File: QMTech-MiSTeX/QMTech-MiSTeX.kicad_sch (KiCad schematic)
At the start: 20 parts, among them J1 RPi_GPIO, J2 MiSTer SDRAM Module, J3 Conn_02x32_Odd_Even, J4 Conn_02x32_Odd_Even, J5 Conn_01x06_Male, J7 Conn_01x05_Pin, J8 USB_C_Receptacle_USB2.0, U5 ZGY133/T10(PLT)

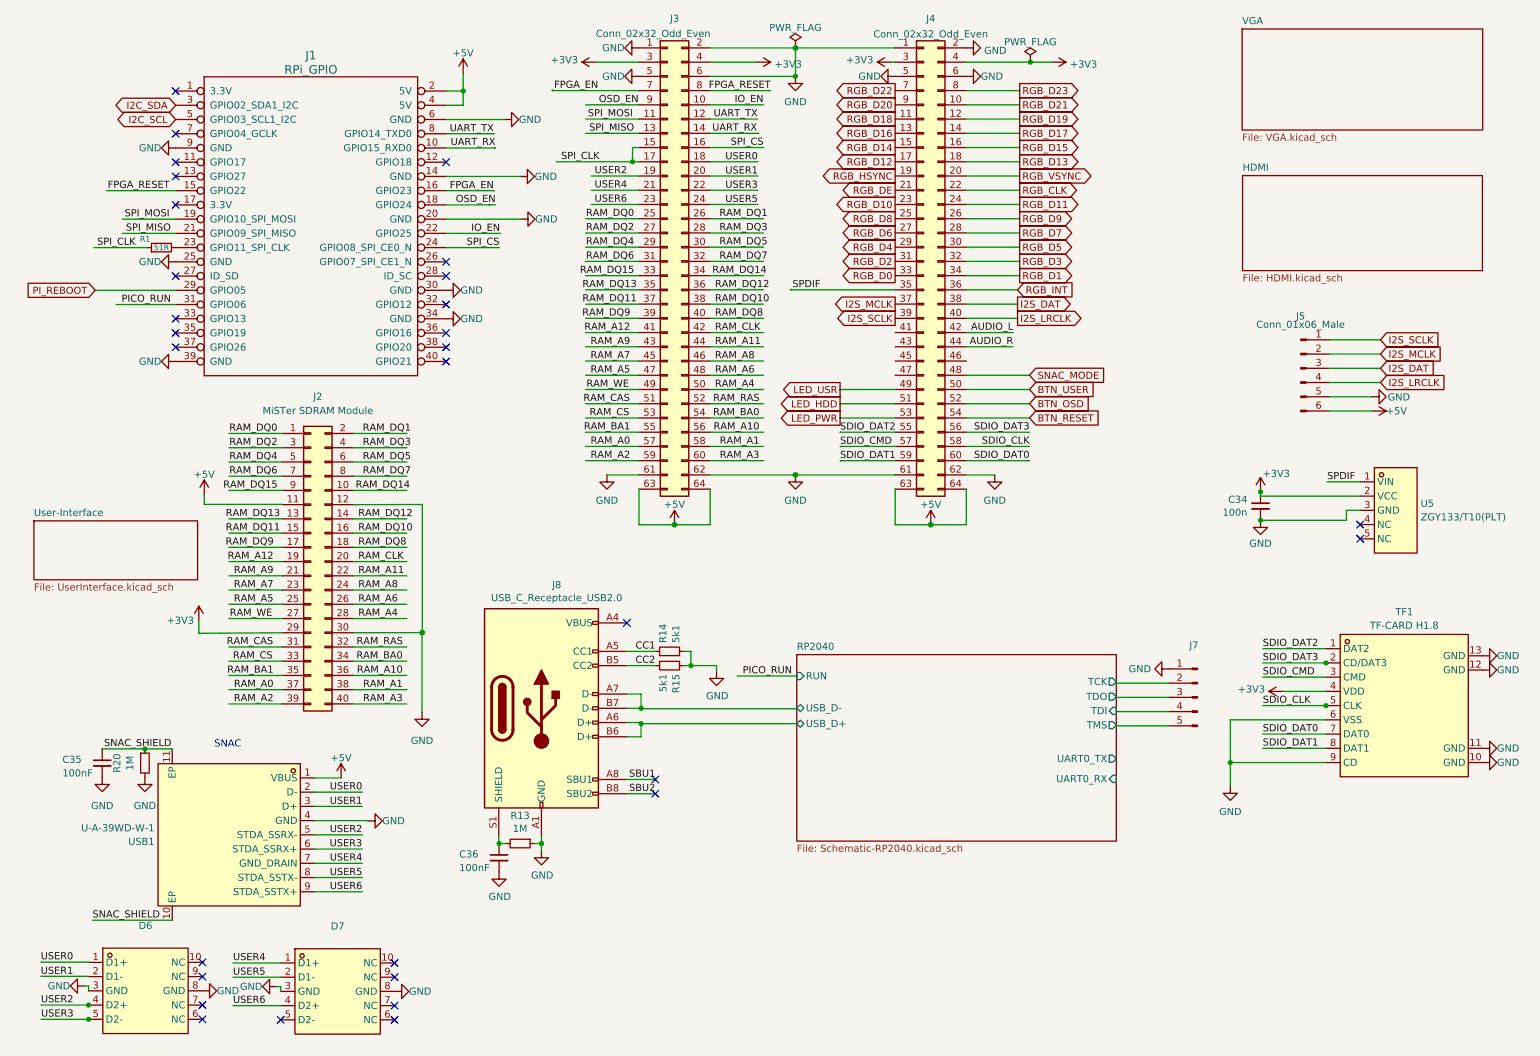
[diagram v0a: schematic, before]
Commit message: move SNAC into its own sheet
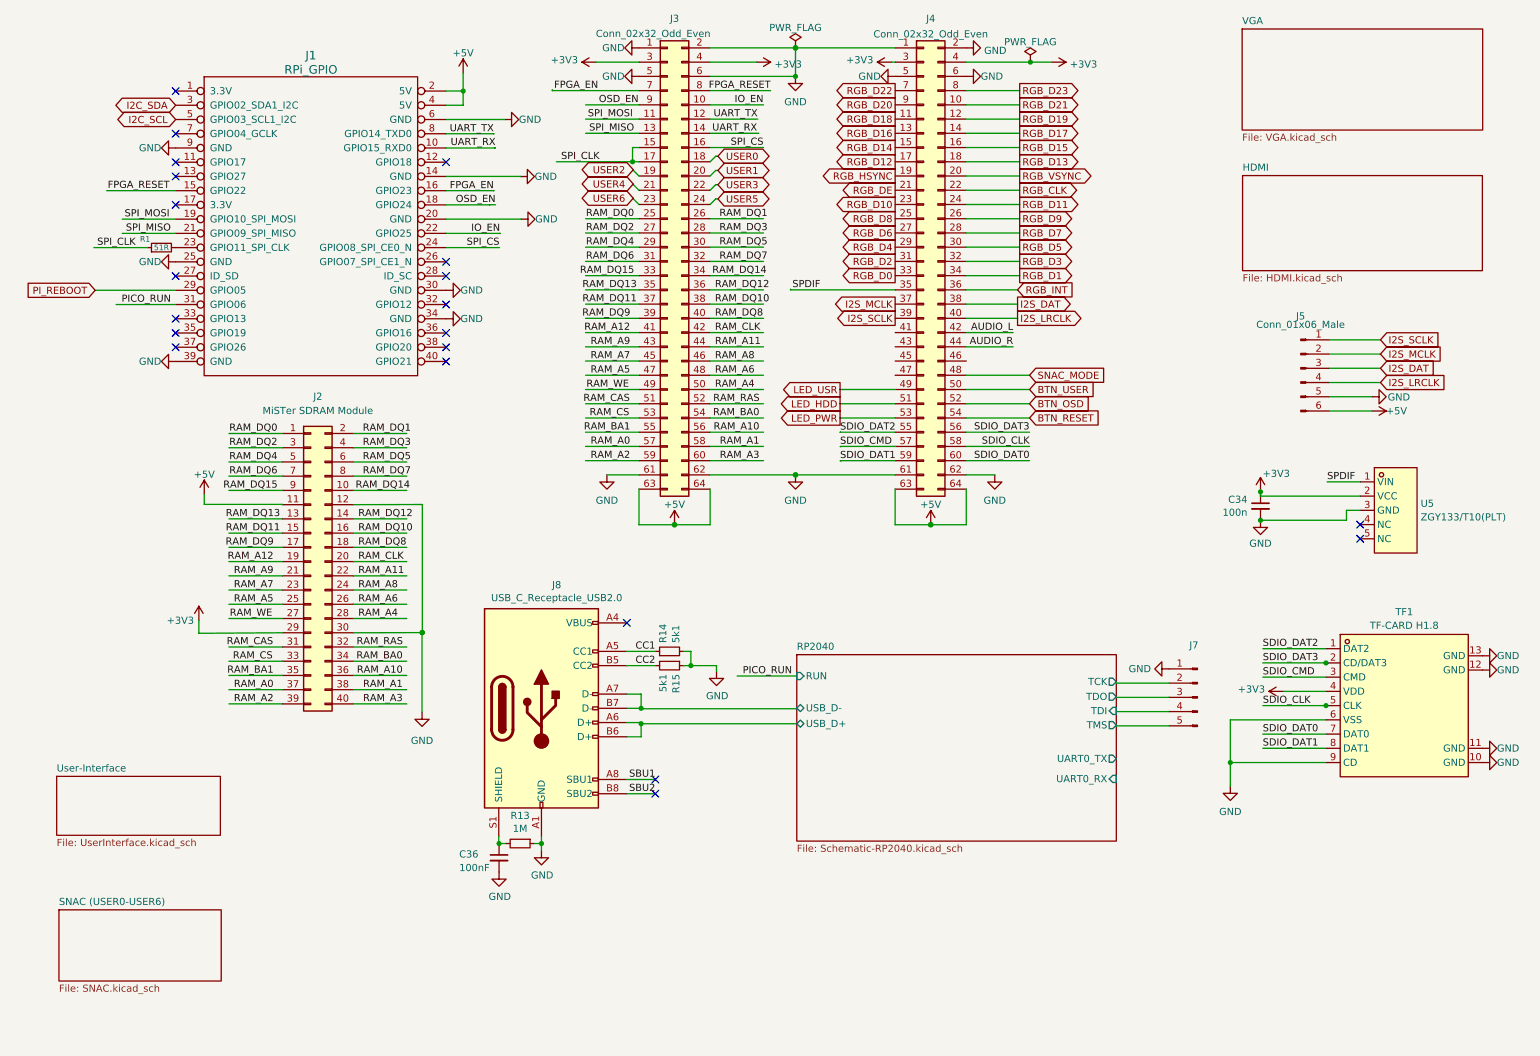
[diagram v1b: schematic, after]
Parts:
- removed C35: 100nF, C_0402_1005Metric, symbol jlcpcb-basic-mlcc-0402:100nF
- removed D6, D7: TPD4E05U06DQAR_C2972498, easyeda2kicad:DFN2510-10_L2.5-W1.0-P0.50-BL, symbol easyeda2kicad:TPD4E05U06DQAR_C2972498
- removed R20: 1M, Resistor_SMD:R_0603_1608Metric, symbol Device:R_Small
- removed USB1: U-A-39WD-W-1, easyeda2kicad:USB-A-SMD_U-A-39WD-W-1, symbol easyeda2kicad:U-A-39WD-W-1
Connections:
- net USER0: now also J3.18 (Pin_18)
- net USER1: now also J3.20 (Pin_20)
- net USER3: now also J3.22 (Pin_22)
- net USER5: now also J3.24 (Pin_24)
- no-connect marks 30 -> 21
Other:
- added sheet SNAC (USER0-USER6) (SNAC.kicad_sch)
- note removed: "SNAC"

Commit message: apply review notes from somhi, move audio into its own subsheet, add analog audio out
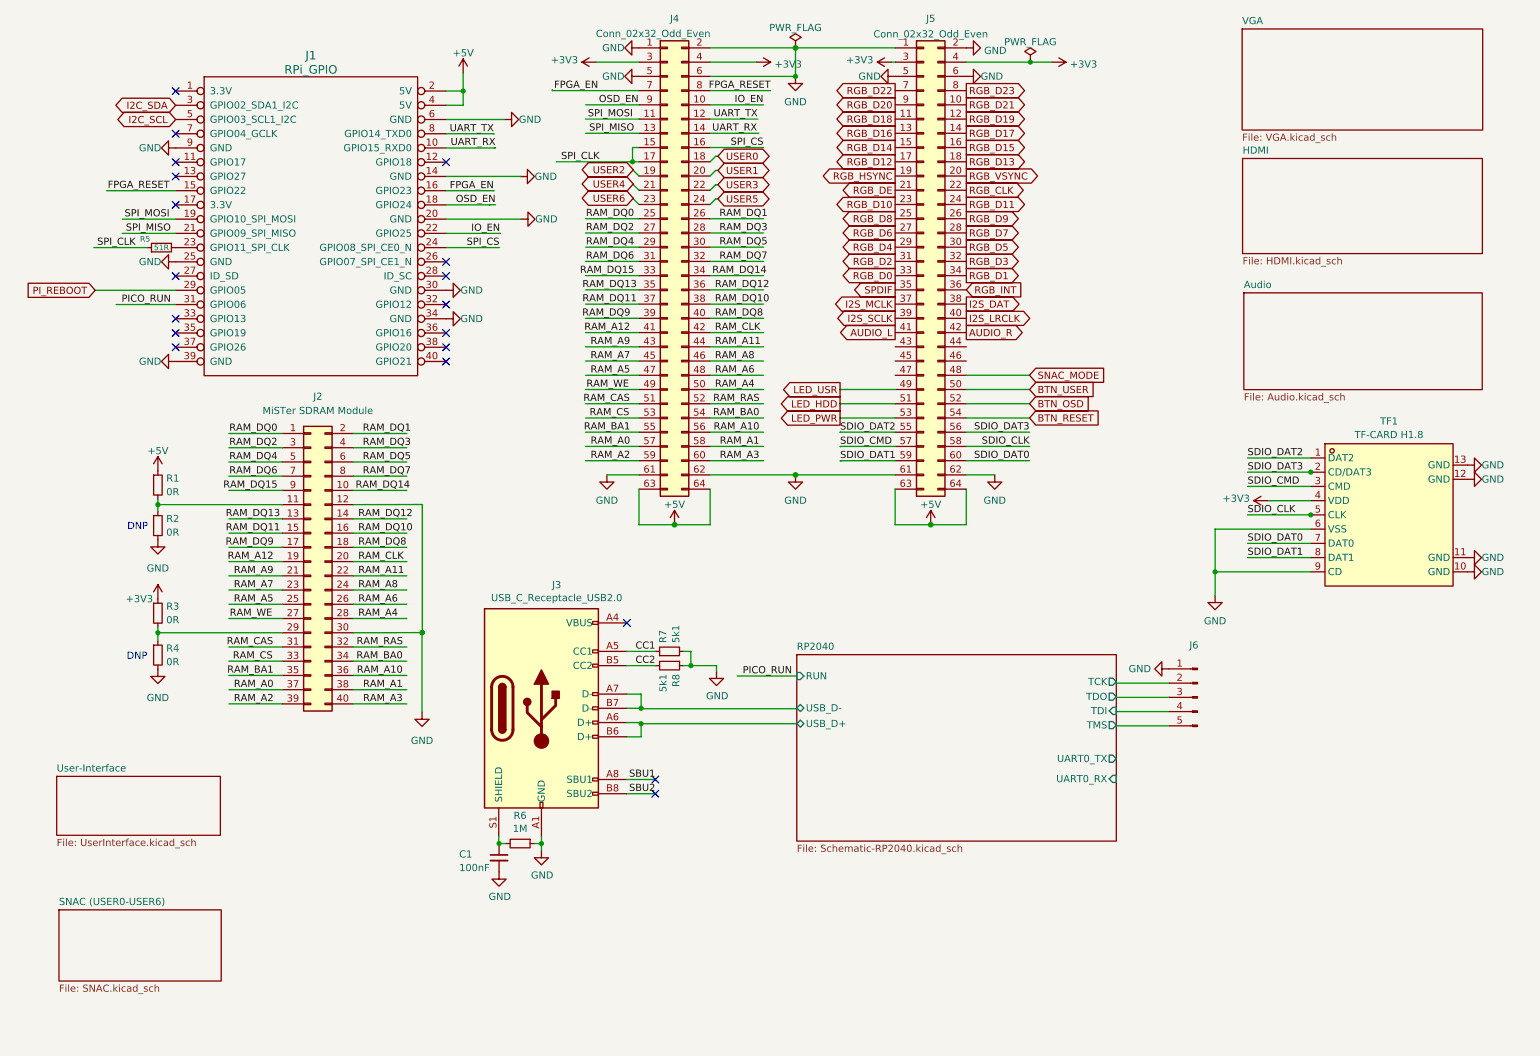
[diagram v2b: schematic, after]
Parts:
- removed C34: 100n, Capacitor_SMD:C_0603_1608Metric, symbol Device:C_Small
- removed J5: Conn_01x06_Male, Connector_PinHeader_2.54mm:PinHeader_1x06_P2.54mm_Vertical, symbol Connector:Conn_01x06_Male
- removed U5: ZGY133/T10(PLT), easyeda2kicad:COMM-TH_ZGY133-T10-PLT, symbol easyeda2kicad:ZGY133_T10(PLT)
- added R1, R2, R3, R4: 0R, R_0402_1005Metric, symbol jlcpcb-basic-resistor-0402:0R
- renumbered C36 to C1, J8 to J3, J3 to J4, J4 to J5, J7 to J6, R1 to R5, R13 to R6, R14 to R7, R15 to R8
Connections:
- net +3V3: now also R3.1; no longer J2.29 (Pin_29)
- net +5V: now also R1.1; no longer J2.11 (Pin_11)
- net AUDIO_L: now also J5.41 (Pin_41); no longer J5.42 (Pin_42)
- net AUDIO_R: now also J5.42 (Pin_42); no longer J5.44 (Pin_44)
- net GND: now also R2.2, R4.2
- new net: J2.29 (Pin_29), R3.2, R4.1
- new net: J2.11 (Pin_11), R1.2, R2.1
- no-connect marks 21 -> 19
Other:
- added sheet Audio (Audio.kicad_sch)
- note added: "DNP"
- moved on the sheet: TF1

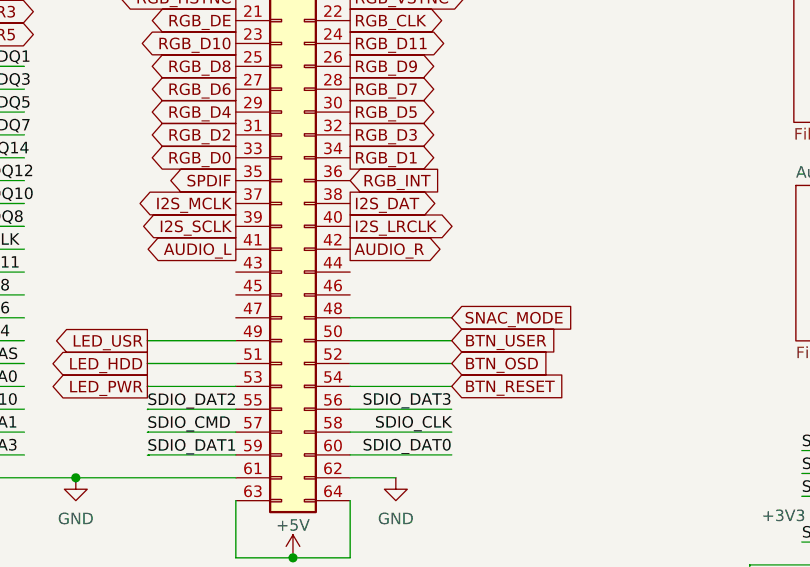
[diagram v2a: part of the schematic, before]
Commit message: add I2C to FPGA pins
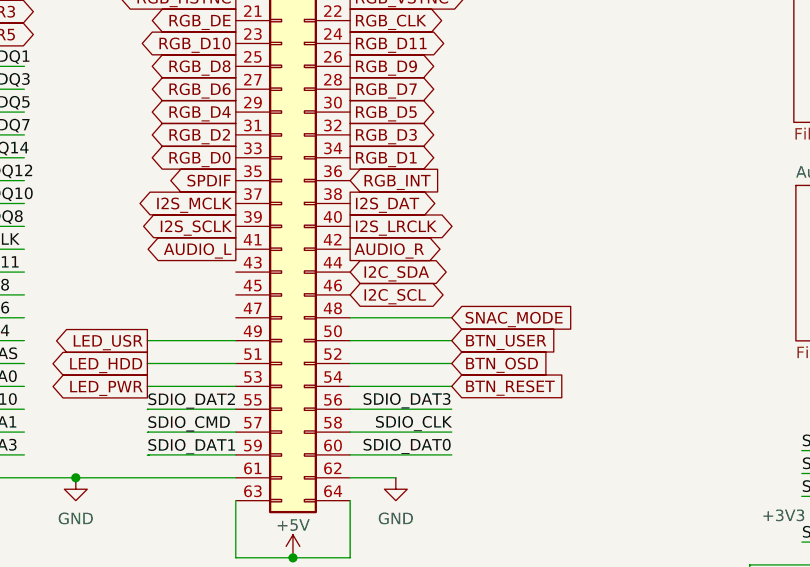
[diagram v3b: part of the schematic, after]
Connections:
- net I2C_SCL: now also J5.46 (Pin_46)
- net I2C_SDA: now also J5.44 (Pin_44)
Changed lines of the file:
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@@
+    )
+  )
+  (global_label "I2C_SDA" (shape bidirectional) (at 181.991 72.3646 0) (fields_autoplaced)
+    (effects (font (size 1.27 1.27)) (justify left))
+    (property "Intersheetrefs" "${INTERSHEET_REFS}" (at 193.7073 72.3646 0)
+      (effects (font (size 1.27 1.27)) (justify left))
     )
   )
@@
     )
   )
+  (global_label "I2C_SCL" (shape bidirectional) (at 181.991 74.9046 0) (fields_autoplaced)
+    (effects (font (size 1.27 1.27)) (justify left))
+    (property "Intersheetrefs" "${INTERSHEET_REFS}" (at 193.6468 74.9046 0)
+      (effects (font (size 1.27 1.27)) (justify left))
+    )
+  )

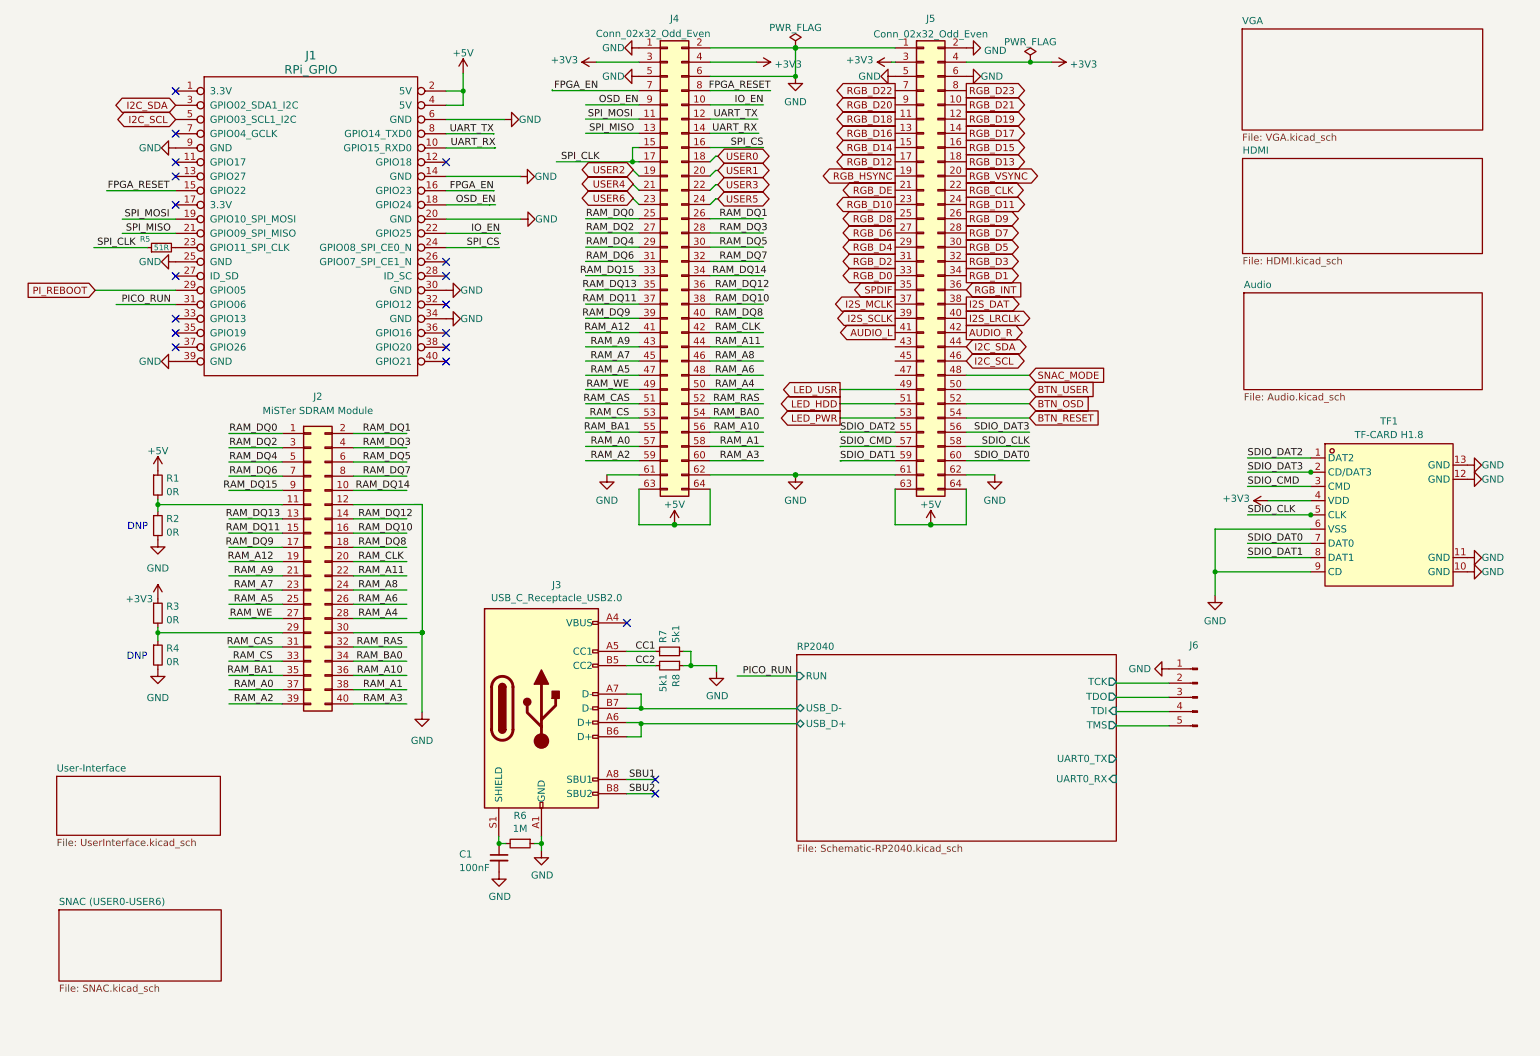
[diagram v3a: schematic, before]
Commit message: add UART connections
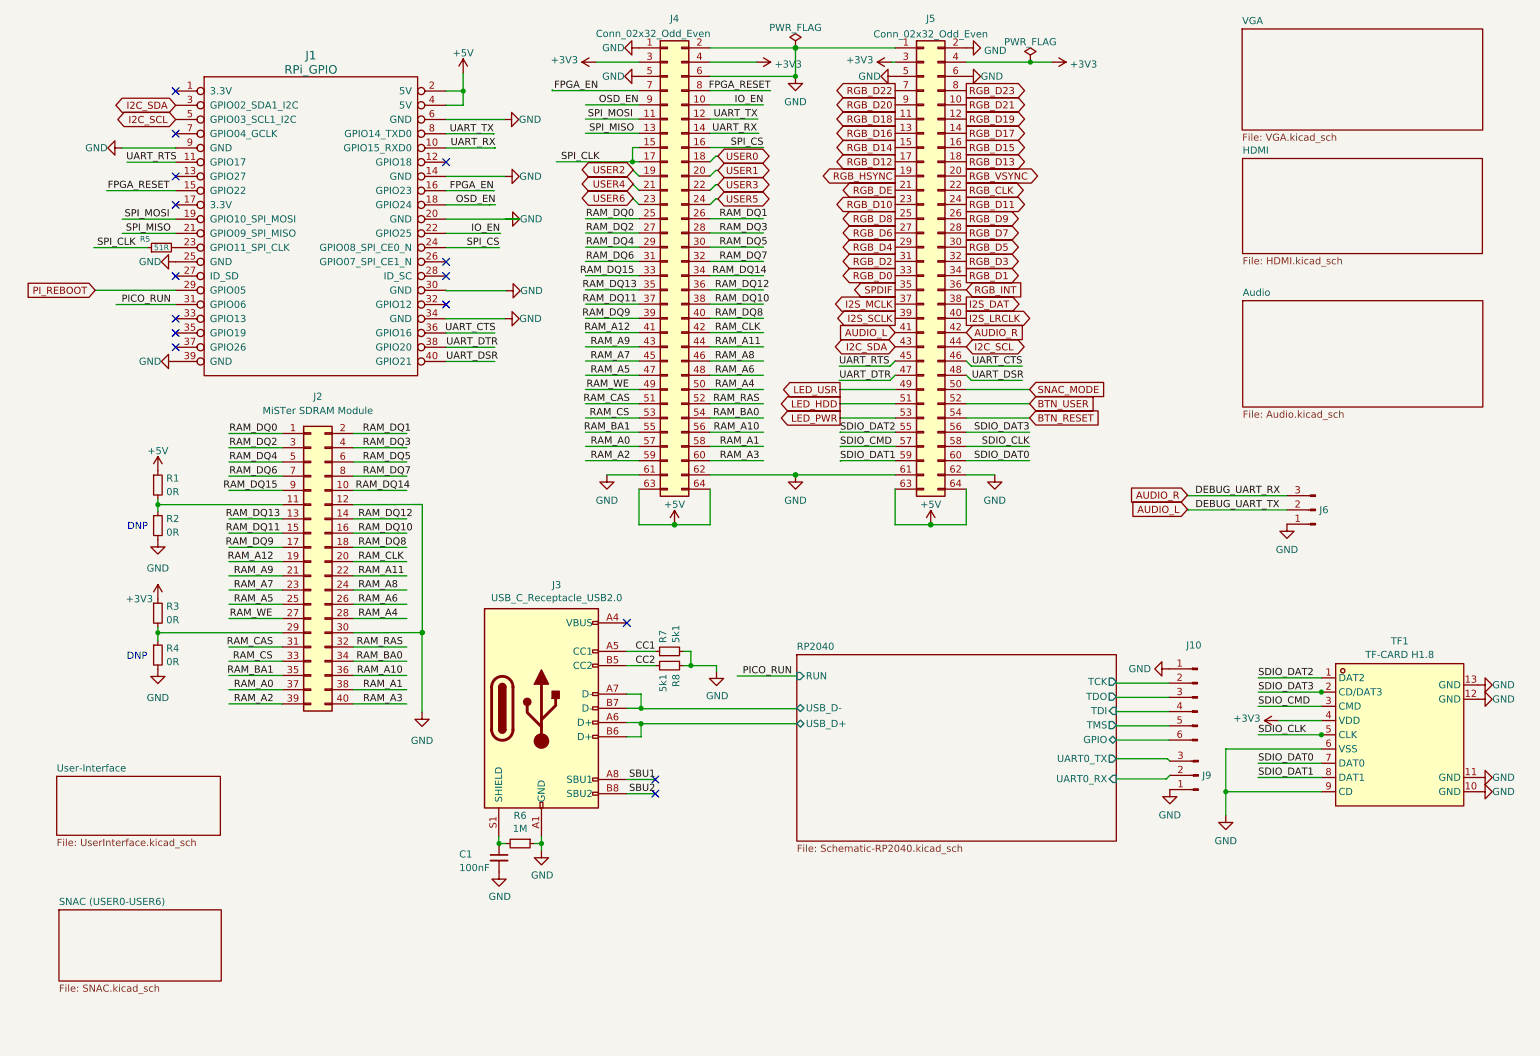
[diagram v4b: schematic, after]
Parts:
- removed J6: Conn_01x05_Pin, symbol Connector:Conn_01x05_Pin
- added J10: Conn_01x06_Pin, Connector_PinHeader_2.54mm:PinHeader_1x06_P2.54mm_Vertical, symbol Connector:Conn_01x06_Pin
- added J6, J9: Conn_01x03_Pin, Connector_PinHeader_2.54mm:PinHeader_1x03_P2.54mm_Vertical, symbol Connector:Conn_01x03_Pin
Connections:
- net BTN_OSD is gone; now on net BTN_USER: J5.52 (Pin_52)
- net AUDIO_L: now also J6.2 (Pin_2)
- net AUDIO_R: now also J6.3 (Pin_3)
- net BTN_USER: no longer J5.50 (Pin_50)
- net GND: now also J10.1 (Pin_1), J6.1 (Pin_1), J9.1 (Pin_1)
- net I2C_SCL: now also J5.44 (Pin_44); no longer J5.46 (Pin_46)
- net I2C_SDA: now also J5.43 (Pin_43); no longer J5.44 (Pin_44)
- net RP2040/TCK: now also J10.2 (Pin_2)
- net RP2040/TDI: now also J10.4 (Pin_4)
- net RP2040/TDO: now also J10.3 (Pin_3)
- net RP2040/TMS: now also J10.5 (Pin_5)
- net RP2040/UART0_RX: now also J9.2 (Pin_2)
- net RP2040/UART0_TX: now also J9.3 (Pin_3)
- net SNAC_MODE: now also J5.50 (Pin_50); no longer J5.48 (Pin_48)
- net UART_DTR: now reaches J1.38 (GPIO20)
- net UART_DTR: now also J5.47 (Pin_47)
- net UART_DSR: now reaches J1.40 (GPIO21)
- net UART_DSR: now also J5.48 (Pin_48)
- net UART_RTS: now reaches J5.45 (Pin_45)
- new net RP2040/GPIO: J10.6 (Pin_6)
- new net UART_CTS: J5.46 (Pin_46)
- no-connect marks 19 -> 15
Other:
- sheet RP2040 ports: added GPIO; removed none
- moved on the sheet: TF1
